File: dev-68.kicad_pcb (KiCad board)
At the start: 2 copper layers, 340 x 187.5 mm, 239 parts, among them J1 Columns, J2 Rows, J3 Columns, J4 Rows, J5 Columns, J6 Rows, J7 LED Drivers, J8 Power, J9 RPI, U1 IS31FL3733-TQ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

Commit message: Small fixes
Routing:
- net GND: track 386.0 -> 391.0 mm

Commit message: Rounded edges
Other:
- board size 340 x 187.5 mm -> 336.6 x 188.1 mm
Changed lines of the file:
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@@
   (general
     (thickness 1.6)
-    (drawings 159)
+    (drawings 162)
     (tracks 3972)
     (zones 0)
@@
     (pad "" np_thru_hole circle (at 2.54 -5.08 180) (size 3 3) (drill 3) (layers *.Cu *.Mask))
   )
+  (gr_arc (start 340.51875 107.15625) (end 340.51875 115.09375) (angle -90) (layer Edge.Cuts) (width 0.05))
+  (gr_arc (start 19.84375 107.15625) (end 11.90625 107.15625) (angle -90) (layer Edge.Cuts) (width 0.05))
+  (gr_arc (start 19.84375 -65.0875) (end 19.84375 -73.025) (angle -90) (layer Edge.Cuts) (width 0.05))
+  (gr_arc (start 340.51875 -65.0875) (end 348.45625 -65.0875) (angle -90) (layer Edge.Cuts) (width 0.05))
   (gr_line (start 302.895 8.09625) (end 305.435 8.128) (layer F.SilkS) (width 0.12))
   (gr_text SW2 (at 226.441 -67.02425 90) (layer F.SilkS)
@@
     (effects (font (size 4 4) (thickness 0.3)))
   )
-  (gr_text "DEV-68\nDEVELOPMENT KEYBOARD\nREV A0" (at 13.335 -69.215) (layer F.SilkS)
+  (gr_text "DEV-68\nDEVELOPMENT KEYBOARD\nREV A0" (at 15.08125 -67.46875) (layer F.SilkS)
     (effects (font (size 1 1) (thickness 0.15)) (justify left))
   )
@@
     (effects (font (size 1 1) (thickness 0.15)))
   )
-  (gr_line (start 350 112.5) (end 97.5 112.5) (layer Edge.Cuts) (width 0.05))
-  (gr_line (start 350 -75) (end 350 112.5) (layer Edge.Cuts) (width 0.05))
-  (gr_line (start 10 -75) (end 350 -75) (layer Edge.Cuts) (width 0.05))
-  (gr_line (start 10 112.5) (end 10 -75) (layer Edge.Cuts) (width 0.05))
-  (gr_line (start 97.5 112.5) (end 10 112.5) (layer Edge.Cuts) (width 0.05))
+  (gr_line (start 340.51875 115.09375) (end 19.84375 115.09375) (layer Edge.Cuts) (width 0.05))
+  (gr_line (start 348.45625 -65.0875) (end 348.45625 107.15625) (layer Edge.Cuts) (width 0.05))
+  (gr_line (start 19.84375 -73.025) (end 340.51875 -73.025) (layer Edge.Cuts) (width 0.05))
+  (gr_line (start 11.90625 107.15625) (end 11.90625 -65.0875) (layer Edge.Cuts) (width 0.05))
   (segment (start 18.3666 33.3875) (end 18.3563 33.3978) (width 0.25) (layer F.Cu) (net 1))
   (segment (start 18.3563 33.3978) (end 18.3563 34.925) (width 0.25) (layer F.Cu) (net 1) (status 20))

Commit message: Fix exposed traces
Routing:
- net B_CS4: track 73.8 -> 69.4 mm
- net GND: track 391.0 -> 394.2 mm
- net B_CS12: track 50.3 -> 52.9 mm
- net B_CS15: track 46.3 -> 48.9 mm
- net B_CS14: track 48.4 -> 50.9 mm
- net B_CS11: track 52.6 -> 54.9 mm
- net B_CS10: track 54.6 -> 56.8 mm
- net B_CS9: track 55.8 -> 57.9 mm, vias 1 -> 0
- net B_CS16: track 44.2 -> 46.1 mm
- net B_CS8: track 57.5 -> 59.3 mm
- net B_CS7: track 60.2 -> 61.7 mm
- net B_CS6: track 63.0 -> 64.4 mm
- net B_CS5: track 65.7 -> 67.2 mm
- net VCC: track 212.1 -> 213.4 mm
- net B_CS13: track 53.7 -> 52.8 mm, vias 2 -> 0
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
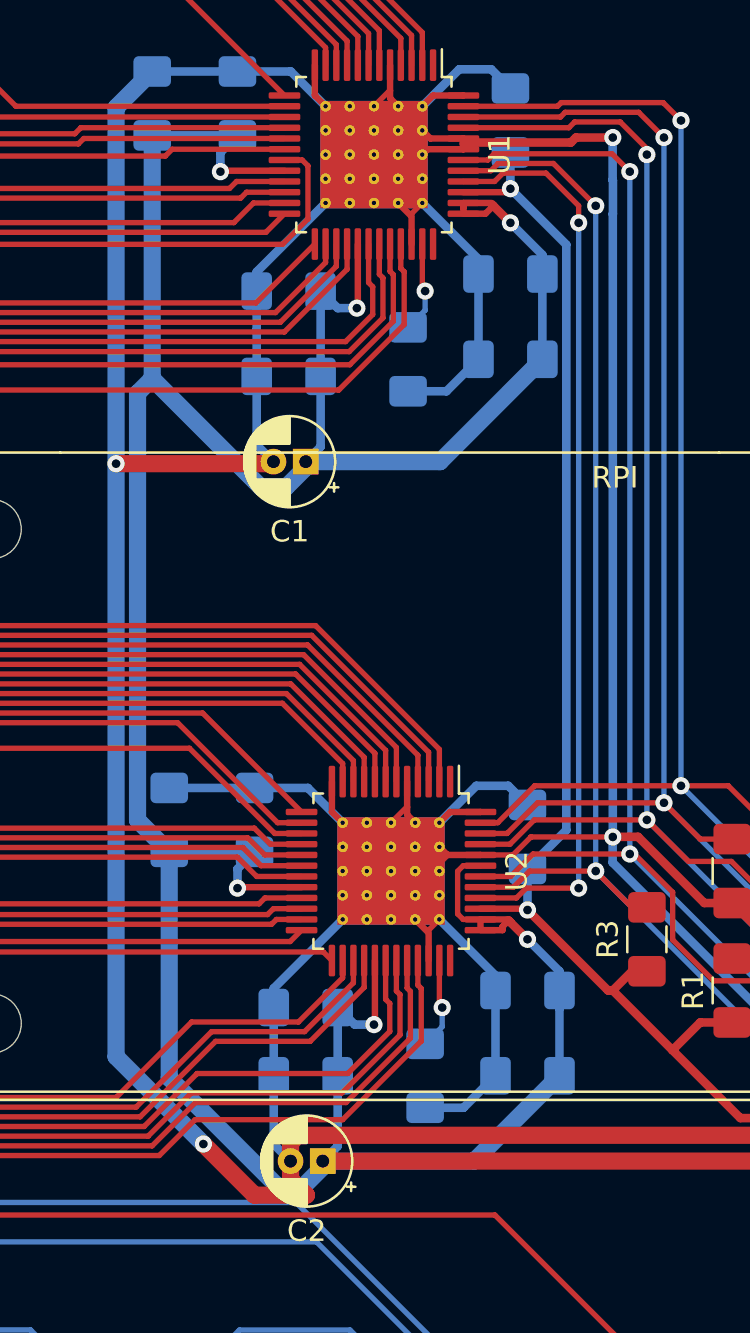
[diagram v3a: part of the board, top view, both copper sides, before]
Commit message: Disconnect one side of GND guarding I2C bus. Clean up C1 & C2 traces.
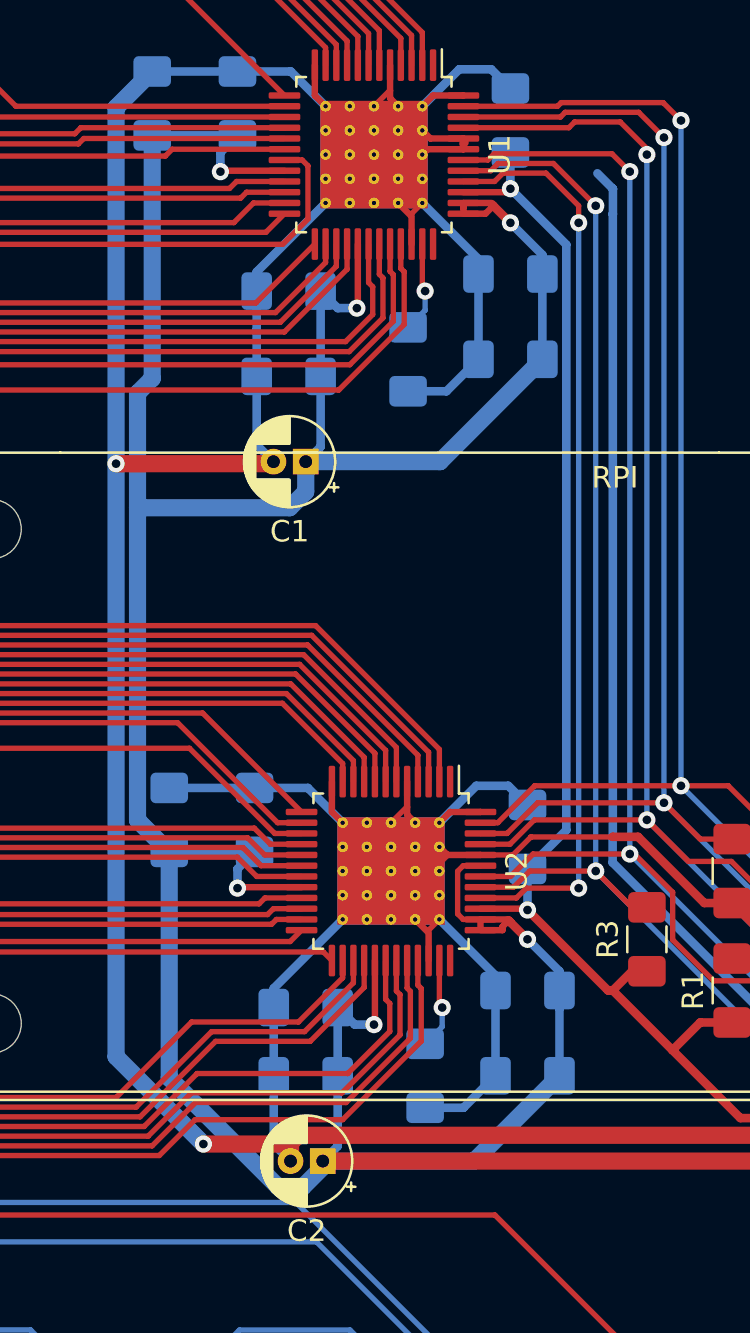
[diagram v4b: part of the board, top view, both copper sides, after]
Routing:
- net GND: track 394.2 -> 382.7 mm, vias 4 -> 2

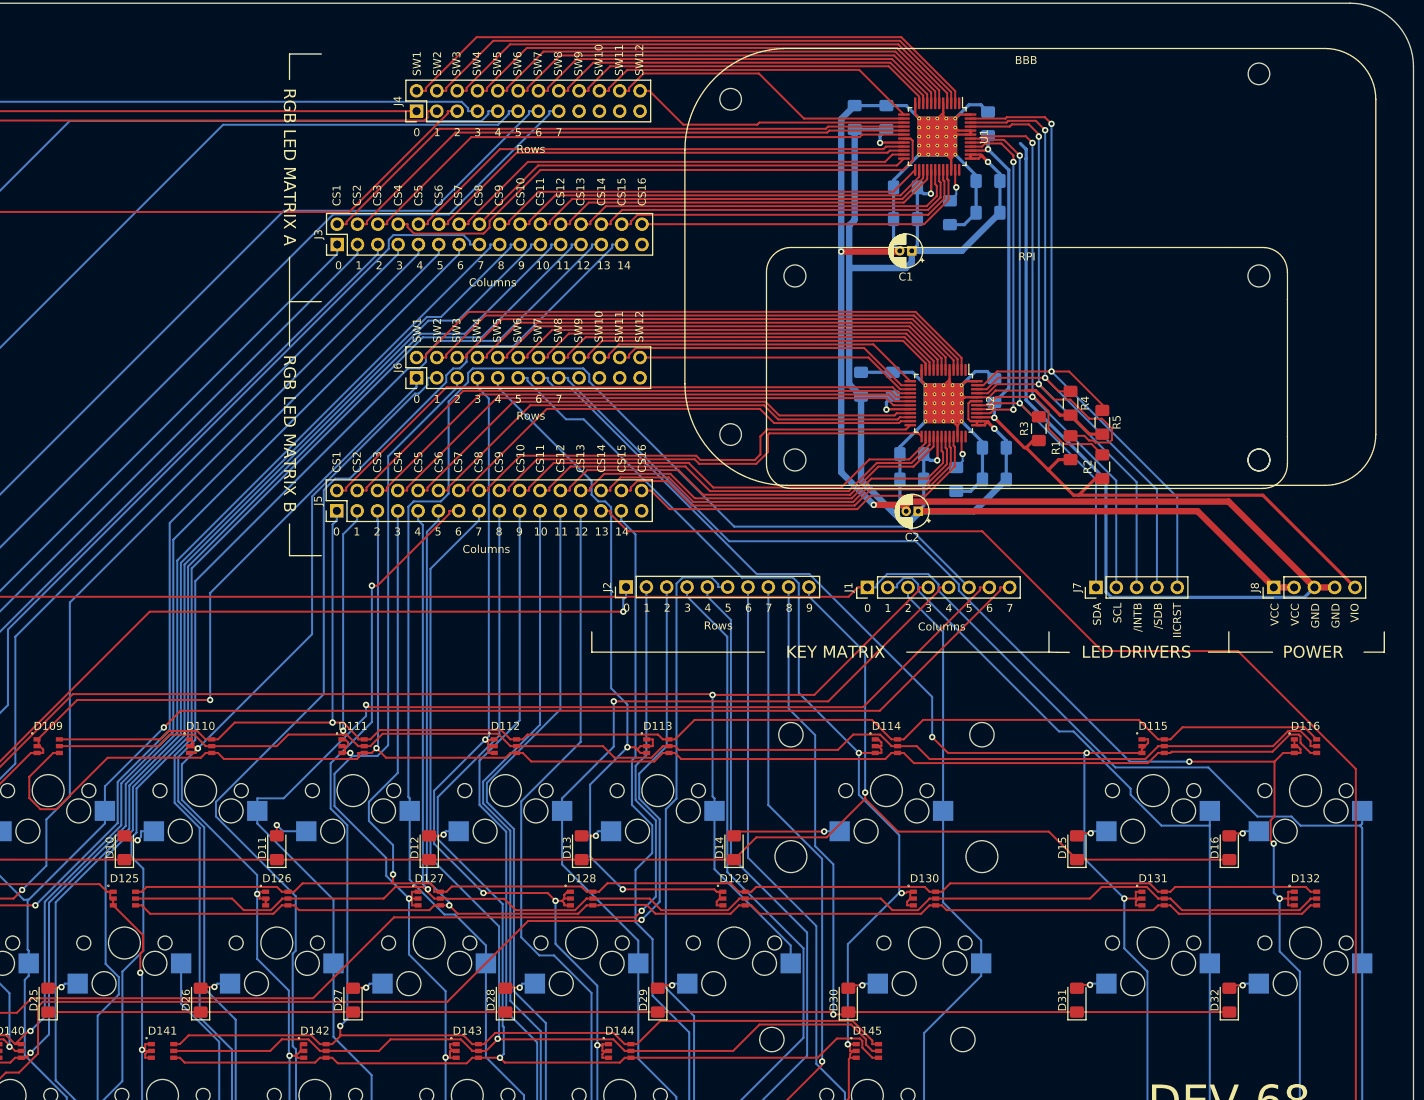
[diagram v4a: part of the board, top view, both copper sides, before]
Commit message: Fix DRC errors.
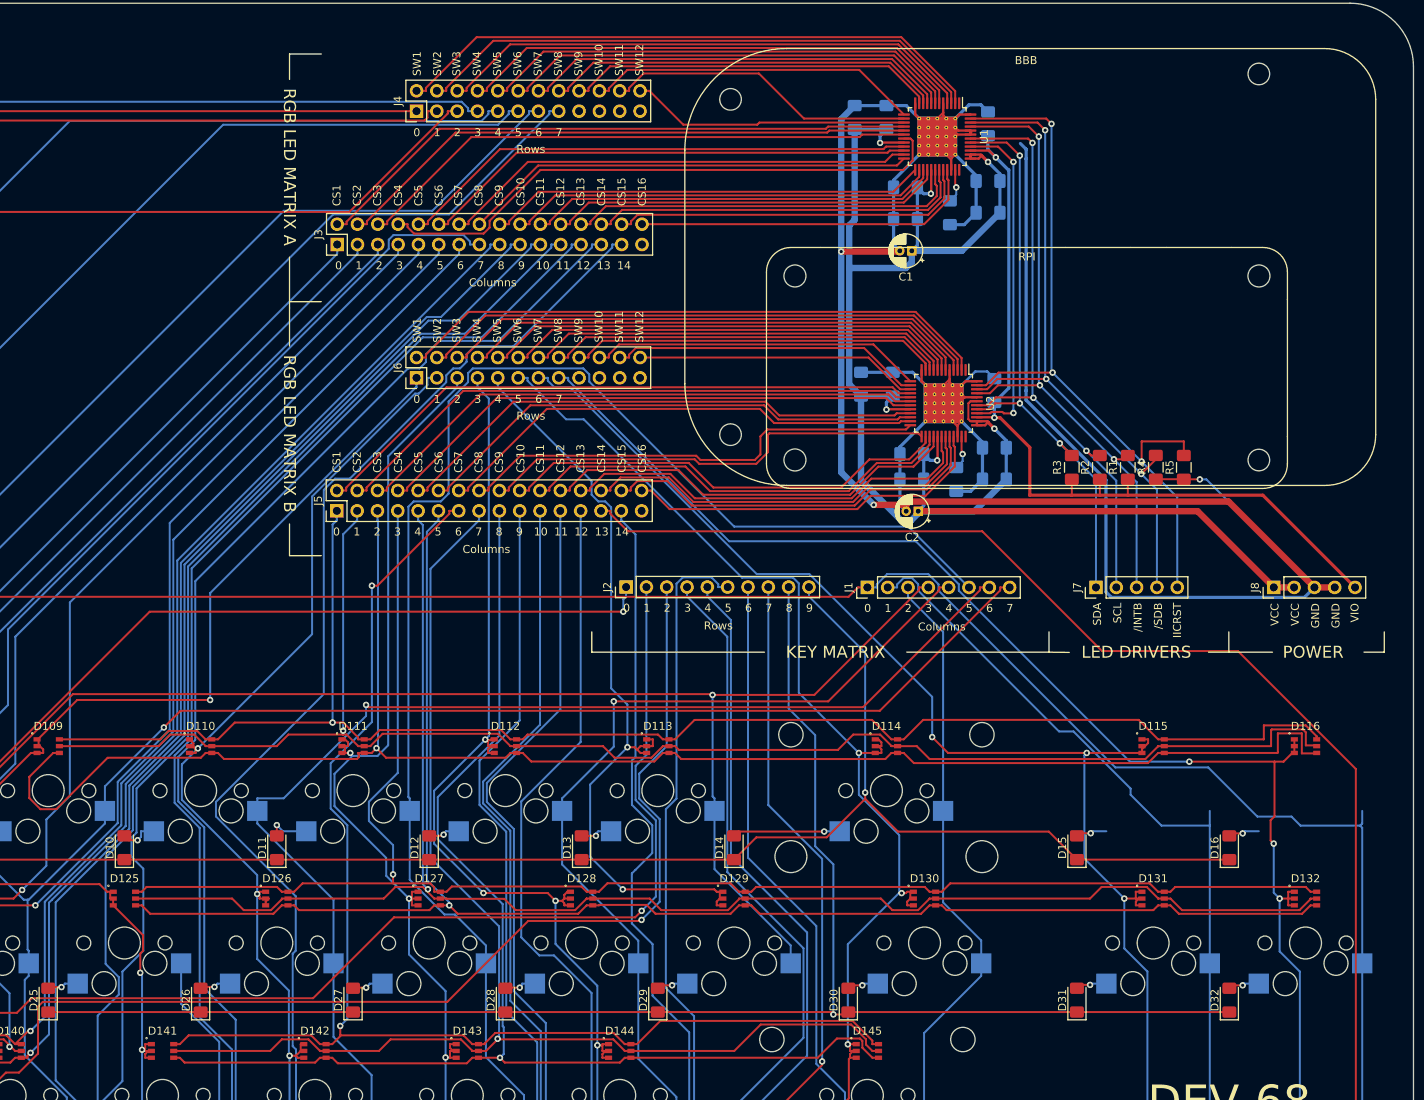
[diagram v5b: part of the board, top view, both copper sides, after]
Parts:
- removed MX15, MX16: MX-NoLED, MX_Only:MXOnly-1U-Hotswap
- moved R4 13.3 mm to (316.2, -15.0)
- moved R5 11.6 mm to (319.8, -15.0)
- moved R1 7.57 mm to (312.8, -15.0)
- moved R3 6.36 mm to (305.8, -15.0)
- moved R2 0.32 mm to (309.2, -15.0)
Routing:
- net INTB: track 97.6 -> 81.0 mm, vias 2 -> 3
- net SCL: track 88.5 -> 77.3 mm, vias 2 -> 3
- net GND: track 382.7 -> 389.8 mm, vias 2 -> 3
- net LED_B_COL_2: track 208.9 -> 211.4 mm
- net LED_B_COL_1: track 195.7 -> 197.6 mm
- net VIO: track 104.9 -> 106.5 mm
- net LED_B_COL_0: track 193.3 -> 194.8 mm
- net LED_B_ROW_7: track 201.2 -> 199.9 mm
- net SDA: track 73.8 -> 72.6 mm, vias 2 -> 3
- net SDB: track 85.8 -> 84.9 mm, vias 2 -> 3
- net IICRST: track 93.8 -> 94.5 mm, vias 2 -> 3
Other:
- rule trace_min: 0.2 -> 0.127
- rule via_min_size: 0.4 -> 0.6

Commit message: Add JLCPCB order number marker.
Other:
- board text added: "JLCJLCJLCJLC"
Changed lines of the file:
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@@
   (general
     (thickness 1.6)
-    (drawings 162)
+    (drawings 163)
     (tracks 4016)
     (zones 0)
@@
     (34 B.Paste user hide)
     (35 F.Paste user hide)
-    (36 B.SilkS user hide)
+    (36 B.SilkS user)
     (37 F.SilkS user)
     (38 B.Mask user hide)
@@
     (pad "" np_thru_hole circle (at 2.54 -5.08 180) (size 3 3) (drill 3) (layers *.Cu *.Mask))
   )
+  (gr_text JLCJLCJLCJLC (at 331 -69) (layer B.SilkS)
+    (effects (font (size 1 1) (thickness 0.15)) (justify left mirror))
+  )
   (gr_arc (start 340.51875 107.15625) (end 340.51875 115.09375) (angle -90) (layer Edge.Cuts) (width 0.05))

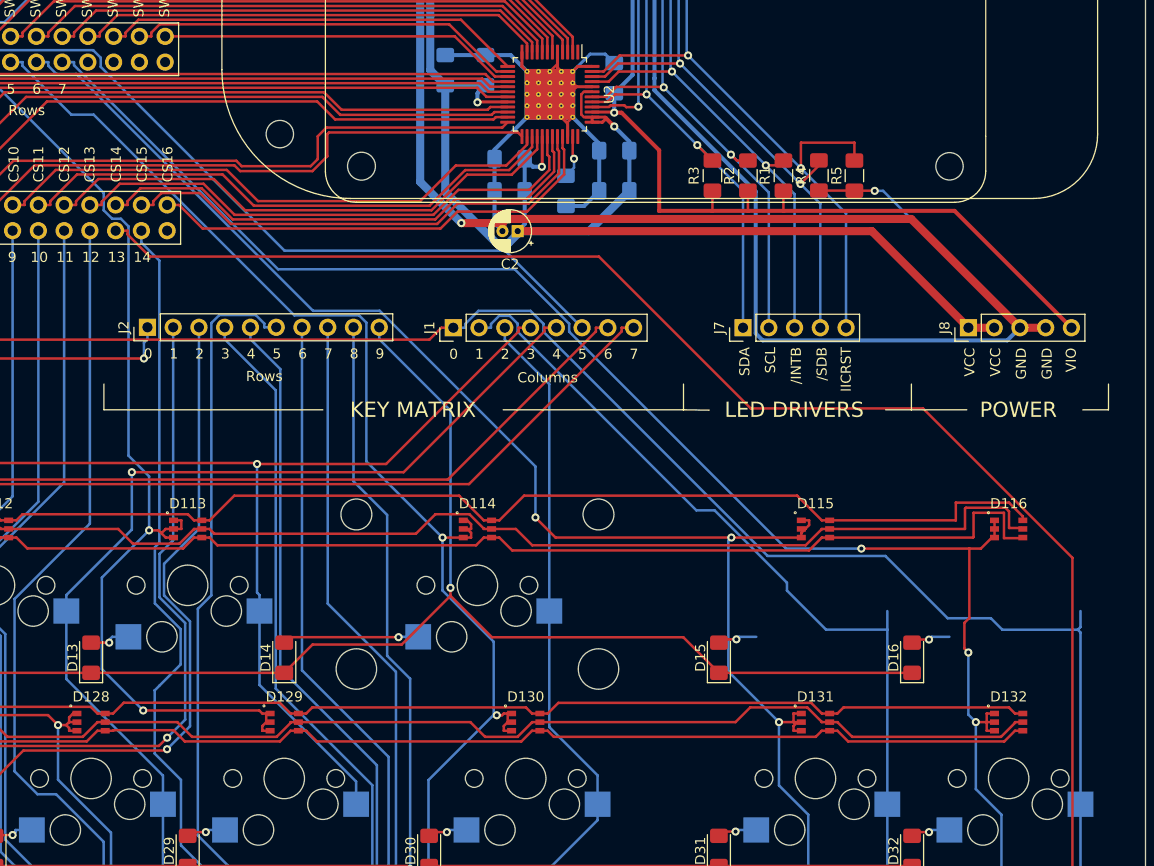
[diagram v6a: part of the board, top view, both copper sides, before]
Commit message: Add keys 15 and 16 back on PCB.
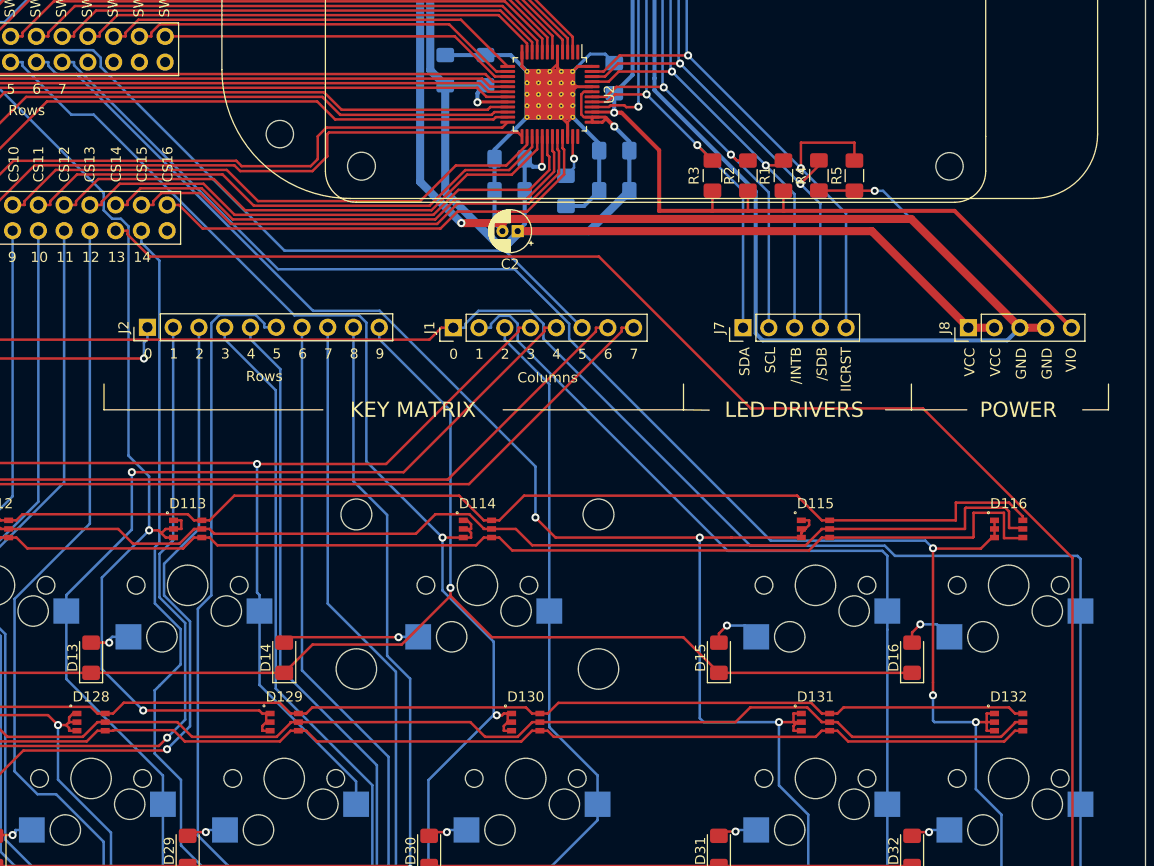
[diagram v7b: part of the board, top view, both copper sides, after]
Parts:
- added MX15: MX-NoLED, MX_Only:MXOnly-1U-Hotswap, F.Cu at (315.9, 25.4)
- added MX16: MX-NoLED, MX_Only:MXOnly-1U-Hotswap, F.Cu at (335.0, 25.4)
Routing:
- net LED_B_ROW_6: track 193.8 -> 199.2 mm
- net LED_B_ROW_7: track 199.9 -> 203.8 mm
- net Net-(D16-Pad2): track 3.92 -> 7.53 mm
- net COL_0: track 495.9 -> 498.6 mm
- net COL_1: track 489.4 -> 492.0 mm
- net Net-(D15-Pad2): track 3.92 -> 5.83 mm
